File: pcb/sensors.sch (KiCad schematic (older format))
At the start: 13 parts, among them J2 I2C_BUS, Q2 BSS138DW-7-F, U4 BME280, U6 SGP30, U7 TSL2591

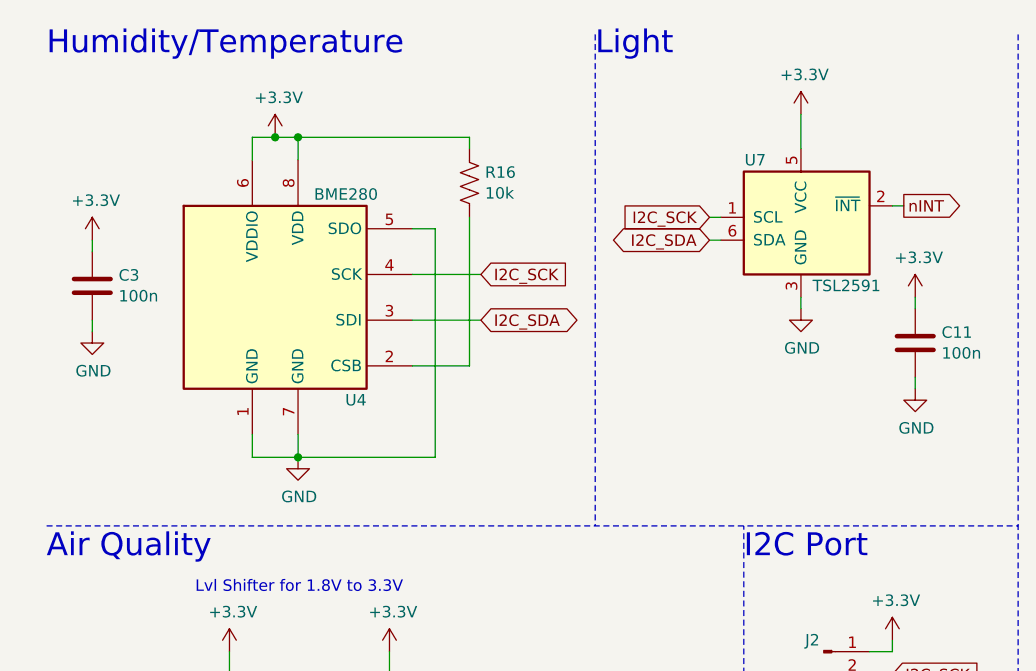
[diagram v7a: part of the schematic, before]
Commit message: use the right tsl2591 footprint
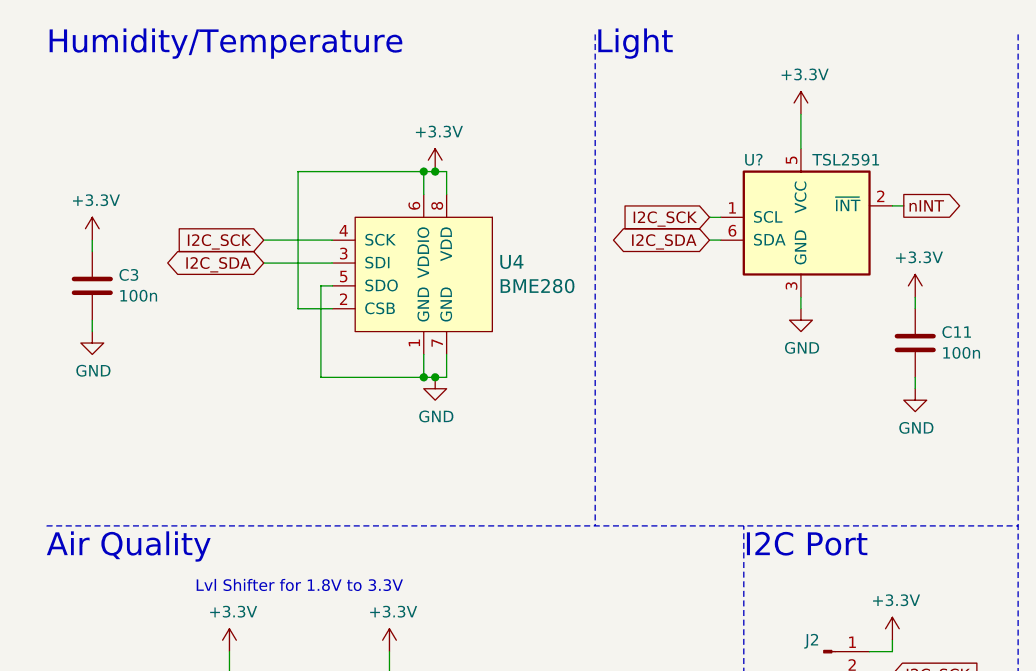
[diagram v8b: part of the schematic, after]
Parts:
- removed R16: 10k, Resistor_SMD:R_0603_1608Metric, symbol Device:R_US
- removed U4: BME280, Package_LGA:Bosch_LGA-8_2.5x2.5mm_P0.65mm_ClockwisePinNumbering, symbol Sensor:BME280
- removed U7: TSL2591, Kevin-Lutzer-Kicad-Lbr:TSL2591, symbol Kevin_Lutzer:TSL2591
- added U4: BME280, digikey-footprints:Pressure_Sensor_LGA-8_2.5x2.5mm_BME280, symbol dk_Humidity-Moisture-Sensors:BME280
- added U?: TSL2591, Kevin-Lutzer-Kicad-Lbr:TSL2591, symbol Kevin_Lutzer:TSL2591
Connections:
- net +3V3: now also U4.2 (CSB), U4.6 (VDDIO), U4.8 (VDD), U?.5 (VCC)
- net GND: now also U4.1 (GND), U4.5 (SDO), U4.7 (GND), U?.3 (GND)
- net I2C_SCK: now also U4.4 (SCK), U?.1 (SCL)
- net I2C_SDA: now also U4.3 (SDI), U?.6 (SDA)
- net nINT: now also U?.2 (~INT)
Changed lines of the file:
@@
 Comment4 ""
 $EndDescr
-Text GLabel 2400 1550 2    50   Input ~ 0
-I2C_SCK
-Text GLabel 2400 1750 2    50   BiDi ~ 0
-I2C_SDA
 $Comp
 L power:GND #PWR?
@@
 Wire Wire Line
 	4050 4950 4050 5100
-$Comp
-L Sensor:BME280 U4
-U 1 1 5F5E97F8
-P 1500 1650
-F 0 "U4" H 1900 1200 50  0000 R CNN
-F 1 "BME280" H 1950 2100 50  0000 R CNN
-F 2 "Package_LGA:Bosch_LGA-8_2.5x2.5mm_P0.65mm_ClockwisePinNumbering" H 3000 1200 50  0001 C CNN
-F 3 "https://ae-bst.resource.bosch.com/media/_tech/media/datasheets/BST-BME280-DS002.pdf" H 1500 1450 50  0001 C CNN
-	1    1500 1650
-	1    0    0    -1
-$EndComp
-Wire Wire Line
-	1400 1050 1400 950
-Wire Wire Line
-	1600 950  1600 1050
-Wire Wire Line
-	2400 1550 2100 1550
-$Comp
-L power:GND #PWR?
-U 1 1 5F5F0DAC
-P 1600 2350
-AR Path="/5F5F0DAC" Ref="#PWR?"  Part="1"
-AR Path="/5F9A85F1/5F5F0DAC" Ref="#PWR0109"  Part="1"
-F 0 "#PWR0109" H 1600 2100 50  0001 C CNN
-F 1 "GND" H 1605 2177 50  0000 C CNN
-F 2 "" H 1600 2350 50  0001 C CNN
-F 3 "" H 1600 2350 50  0001 C CNN
-	1    1600 2350
-	1    0    0    -1
-$EndComp
-Wire Wire Line
-	1400 2250 1400 2350
-Wire Wire Line
-	1400 2350 1600 2350
-Wire Wire Line
-	1600 2350 1600 2250
-Connection ~ 1600 2350
-$Comp
-L power:+3.3V #PWR?
-U 1 1 5F60BDED
-P 1500 950
-AR Path="/5F60BDED" Ref="#PWR?"  Part="1"
-AR Path="/5F9A85F1/5F60BDED" Ref="#PWR0126"  Part="1"
-F 0 "#PWR0126" H 1500 800 50  0001 C CNN
-F 1 "+3.3V" H 1515 1123 50  0000 C CNN
-F 2 "" H 1500 950 50  0001 C CNN
-F 3 "" H 1500 950 50  0001 C CNN
-	1    1500 950
-	1    0    0    -1
-$EndComp
-Wire Wire Line
-	1400 950  1500 950
-Connection ~ 1500 950
-Wire Wire Line
-	1500 950  1600 950
-$Comp
-L Device:R_US R16
-U 1 1 5F61590D
-P 2350 1150
-F 0 "R16" H 2418 1196 50  0000 L CNN
-F 1 "10k" H 2418 1105 50  0000 L CNN
-F 2 "Resistor_SMD:R_0603_1608Metric" V 2390 1140 50  0001 C CNN
-F 3 "~" H 2350 1150 50  0001 C CNN
-	1    2350 1150
-	1    0    0    -1
-$EndComp
-Wire Wire Line
-	2350 1000 2350 950
-Wire Wire Line
-	2100 1950 2350 1950
-Wire Wire Line
-	2350 1300 2350 1950
-Wire Wire Line
-	1600 950  2350 950
-Connection ~ 1600 950
-Wire Wire Line
-	2100 1750 2400 1750
 Text Notes 700  6350 0    50   ~ 0
 Sensor Address\nBME280 - 0x77\nTSL2591 - 0x29\nSGP30 - 0x58
@@
 Text Notes 3550 4150 0    100  ~ 0
 I2C Bus\nPullups
-Wire Wire Line
-	1600 2350 2200 2350
-Wire Wire Line
-	2200 2350 2200 1350
-Wire Wire Line
-	2200 1350 2100 1350
-$Comp
-L Kevin_Lutzer:TSL2591 U7
-U 1 1 5F50BFF8
+$Comp
+L dk_Humidity-Moisture-Sensors:BME280 U4
+U 1 1 600A75C8
+P 2150 1600
+F 0 "U4" H 2478 1703 60  0000 L CNN
+F 1 "BME280" H 2478 1597 60  0000 L CNN
+F 2 "digikey-footprints:Pressure_Sensor_LGA-8_2.5x2.5mm_BME280" H 2350 1800 60  0001 L CNN
+F 3 "https://ae-bst.resource.bosch.com/media/_tech/media/datasheets/BST-BME280-DS002.pdf" H 2350 1900 60  0001 L CNN
+F 4 "828-1063-1-ND" H 2350 2000 60  0001 L CNN "Digi-Key_PN"
+F 5 "BME280" H 2350 2100 60  0001 L CNN "MPN"
+F 6 "Sensors, Transducers" H 2350 2200 60  0001 L CNN "Category"
+F 7 "Humidity, Moisture Sensors" H 2350 2300 60  0001 L CNN "Family"
+F 8 "https://ae-bst.resource.bosch.com/media/_tech/media/datasheets/BST-BME280-DS002.pdf" H 2350 2400 60  0001 L CNN "DK_Datasheet_Link"
+F 9 "/product-detail/en/bosch-sensortec/BME280/828-1063-1-ND/6136314" H 2350 2500 60  0001 L CNN "DK_Detail_Page"
+F 10 "SENSOR PRESSURE HUMIDITY TEMP" H 2350 2600 60  0001 L CNN "Description"
+F 11 "Bosch Sensortec" H 2350 2700 60  0001 L CNN "Manufacturer"
+F 12 "Active" H 2350 2800 60  0001 L CNN "Status"
+	1    2150 1600
+	1    0    0    -1
+$EndComp
+$Comp
+L power:GND #PWR?
+U 1 1 5FFBEA29
+P 2200 2000
+AR Path="/5FFBEA29" Ref="#PWR?"  Part="1"
+AR Path="/5F9A85F1/5FFBEA29" Ref="#PWR0105"  Part="1"
+F 0 "#PWR0105" H 2200 1750 50  0001 C CNN
+F 1 "GND" H 2205 1827 50  0000 C CNN
+F 2 "" H 2200 2000 50  0001 C CNN
+F 3 "" H 2200 2000 50  0001 C CNN
+	1    2200 2000
+	1    0    0    -1
+$EndComp
+$Comp
+L power:+3.3V #PWR?
+U 1 1 5FFBEED3
+P 2200 1100
+AR Path="/5FFBEED3" Ref="#PWR?"  Part="1"
+AR Path="/5F9A85F1/5FFBEED3" Ref="#PWR0109"  Part="1"
+F 0 "#PWR0109" H 2200 950 50  0001 C CNN
+F 1 "+3.3V" H 2215 1273 50  0000 C CNN
+F 2 "" H 2200 1100 50  0001 C CNN
+F 3 "" H 2200 1100 50  0001 C CNN
+	1    2200 1100
+	1    0    0    -1
+$EndComp
+Wire Wire Line
+	2150 1900 2150 2000
+Wire Wire Line
+	2150 2000 2200 2000
+Wire Wire Line
+	2200 2000 2250 2000
+Wire Wire Line
+	2250 2000 2250 1900
+Connection ~ 2200 2000
+Wire Wire Line
+	2150 1200 2150 1100
+Wire Wire Line
+	2150 1100 2200 1100
+Wire Wire Line
+	2200 1100 2250 1100
+Wire Wire Line
+	2250 1100 2250 1200
+Connection ~ 2200 1100
+Text GLabel 1450 1400 0    50   Input ~ 0
+I2C_SCK
+Text GLabel 1450 1500 0    50   BiDi ~ 0
+I2C_SDA
+Wire Wire Line
+	2150 1100 1600 1100
+Wire Wire Line
+	1600 1100 1600 1700
+Wire Wire Line
+	1600 1700 1750 1700
+Connection ~ 2150 1100
+Wire Wire Line
+	1450 1400 1750 1400
+Wire Wire Line
+	1450 1500 1750 1500
+Wire Wire Line
+	1750 1600 1700 1600
+Wire Wire Line
+	1700 1600 1700 2000
+Wire Wire Line
+	1700 2000 2150 2000
+Connection ~ 2150 2000
+$Comp
+L Kevin_Lutzer:TSL2591 U?
+U 1 1 5FFE72E4
 P 3850 1350
-F 0 "U7" H 3600 1650 50  0000 C CNN
-F 1 "TSL2591" H 4000 1100 50  0000 C CNN
+F 0 "U?" H 3550 1650 50  0000 L CNN
+F 1 "TSL2591" H 3850 1650 50  0000 L CNN
 F 2 "Kevin-Lutzer-Kicad-Lbr:TSL2591" H 3300 1100 50  0001 C CNN
 F 3 "https://cdn-shop.adafruit.com/datasheets/TSL25911_Datasheet_EN_v1.pdf" H 3800 1400 50  0001 C CNN
